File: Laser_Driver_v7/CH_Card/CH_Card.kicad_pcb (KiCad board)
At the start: 6 copper layers, 160 x 100 mm, 192 parts, among them J1 DIN41612_03x32_C_Split, Q13 IRL540N, Q14 IRF9540N, Q17 IRL540N, Q18 IRF9540N, Q19 DMN3404L, U101 AD5696R, U102 ADS1115, U103 PCA9538, U104 ADG419BRM, U105 ADG419BRM, U106 OPA192IDBVR, U107 OPA551U, U108 ADG419BRM, U17 OPA192IDBVR, U19 OPA192IDBVR, U21 OPA551U, U22 OPA192IDBVR, U24 OPA192IDBVR, U26 ADG419BRM, U28 INA828, U32 INA828

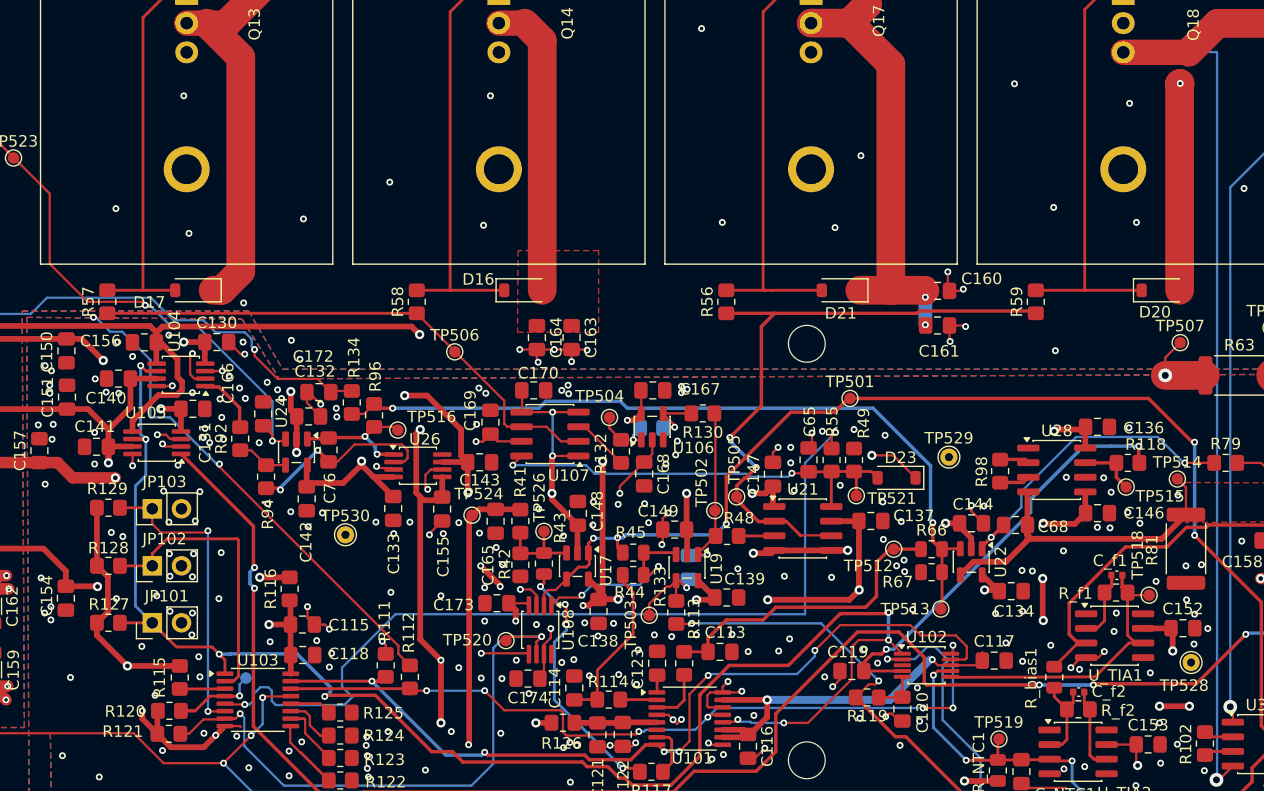
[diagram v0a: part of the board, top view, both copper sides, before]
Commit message: Updates to capacitors for derating.
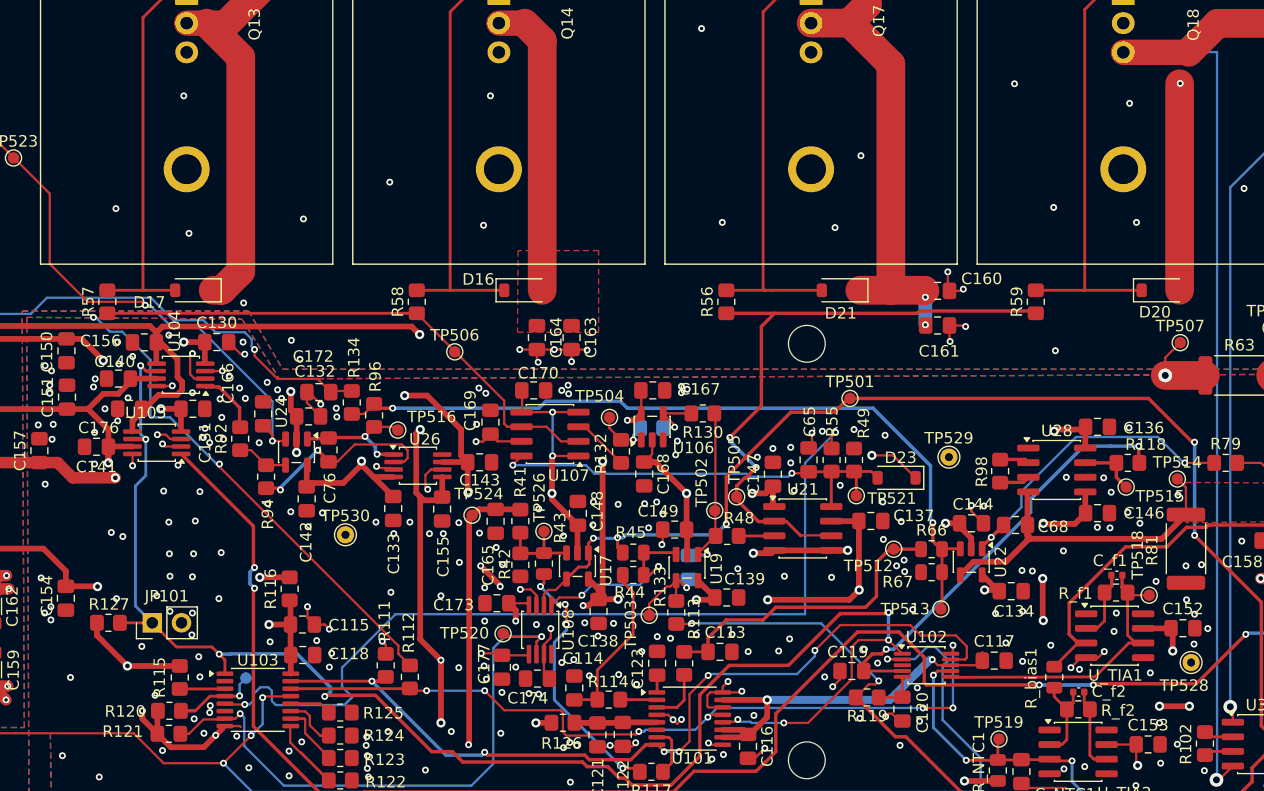
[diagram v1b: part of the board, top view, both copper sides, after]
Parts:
- removed JP102: GA1 addr jumper, Connector_PinHeader_2.54mm:PinHeader_1x02_P2.54mm_Vertical
- removed JP103: GA2 addr jumper, Connector_PinHeader_2.54mm:PinHeader_1x02_P2.54mm_Vertical
- removed R128: 10k GA1 pullup, Resistor_SMD:R_0805_2012Metric_Pad1.20x1.40mm_HandSolder
- removed R129: 10k GA2 pullup, Resistor_SMD:R_0805_2012Metric_Pad1.20x1.40mm_HandSolder
- added C176: 100nF U105 +5V dec, Capacitor_SMD:C_0805_2012Metric_Pad1.18x1.45mm_HandSolder, F.Cu at (90.2, 105.9)
- added C177: 100nF U108 +5V dec, Capacitor_SMD:C_0805_2012Metric_Pad1.18x1.45mm_HandSolder, F.Cu at (122.6, 128.4)
- C76: value Ci 1n -> Ci 1n C0G
- moved C174 0.83 mm to (125.7, 129.3)
- moved TP520 0.65 mm to (122.7, 125.5)
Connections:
- U103 pad 2: GA1 -> GND
- U103 pad 6: GA2 -> GND
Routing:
- net GA2: track 26.4 -> 0.00 mm, vias 2 -> 0
- net GA1: track 25.1 -> 0.00 mm
- net 3V3_DIG: track 122.3 -> 111.5 mm
- net GND: track 66.9 -> 62.2 mm, vias 260 -> 270
- net -15V: track 247.4 -> 248.4 mm, vias 23 -> 22

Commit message: minor updates and U for FBG
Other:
- board text added: "CH_Card v7"
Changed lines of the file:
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@@
 	)
 	(embedded_fonts no)
+	(gr_text "CH_Card v7"
+		(at 86.850 48.050 0)
+		(layer "B.SilkS")
+		(effects
+			(font
+				(size 1.5 1.5)
+				(thickness 0.25)
+			)
+			(justify mirror)
+		)
+	)
 )
